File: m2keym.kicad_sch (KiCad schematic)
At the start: 14 parts, among them J7 Bus_M.2_1-2199230-6

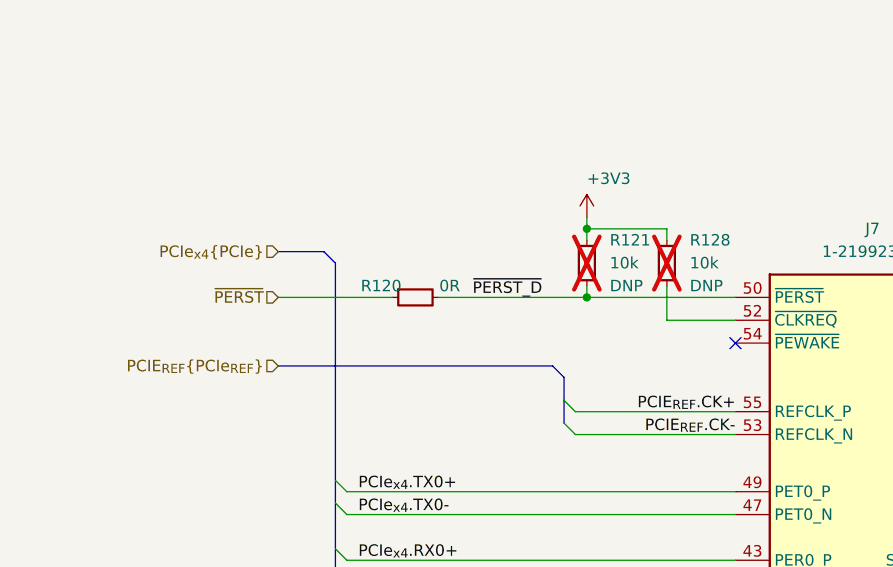
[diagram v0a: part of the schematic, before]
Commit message: [#58904] Change pinout of backplane connector. Connect CLKREQ from PCIe devices
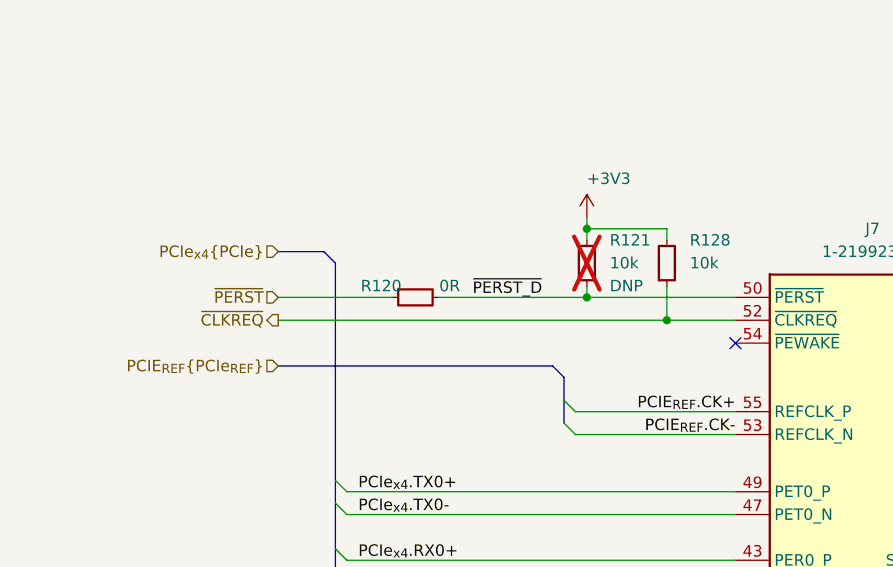
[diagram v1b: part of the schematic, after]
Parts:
- R128: DNP DNP -> (none); now fitted
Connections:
- net ~{CLKREQ}: now reaches J7.52 (~{CLKREQ}), R128.1
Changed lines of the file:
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@@
     (company "Antmicro Ltd.")
+  )
+  (junction (at 193.04 91.44) (diameter 0) (color 0 0 0 0)
   )
   (junction (at 184.15 81.28) (diameter 0) (color 0 0 0 0)
@@
     (stroke (width 0) (type default))
   )
+  (wire (pts (xy 149.86 91.44) (xy 193.04 91.44))
+    (stroke (width 0) (type default))
+  )
   (bus (pts (xy 156.21 134.62) (xy 156.21 139.7))
     (stroke (width 0) (type default))
@@
   )
   (hierarchical_label "PCIe_{x4}{PCIe}" (shape input) (at 149.86 83.82 180) (fields_autoplaced)
+    (effects (font (size 1.27 1.27)) (justify right))
+  )
+  (hierarchical_label "~{CLKREQ}" (shape output) (at 149.86 91.44 180) (fields_autoplaced)
     (effects (font (size 1.27 1.27)) (justify right))
   )
@@
   )
   (symbol (lib_id "antmicroResistors0402:R_10k_0402") (at 193.04 87.63 90) (unit 1)
-    (in_bom yes) (on_board yes) (dnp yes) (fields_autoplaced)
+    (in_bom yes) (on_board yes) (dnp no) (fields_autoplaced)
     (property "Reference" "R128" (at 195.58 82.55 90)
       (effects (font (size 1.27 1.27) (thickness 0.15)) (justify right))
@@
       (effects (font (size 1.27 1.27)) (justify left bottom) hide)
     )
-    (property "DNP" "DNP" (at 195.58 87.63 90)
-      (effects (font (size 1.27 1.27)) (justify right))
-    )
     (pin "2")

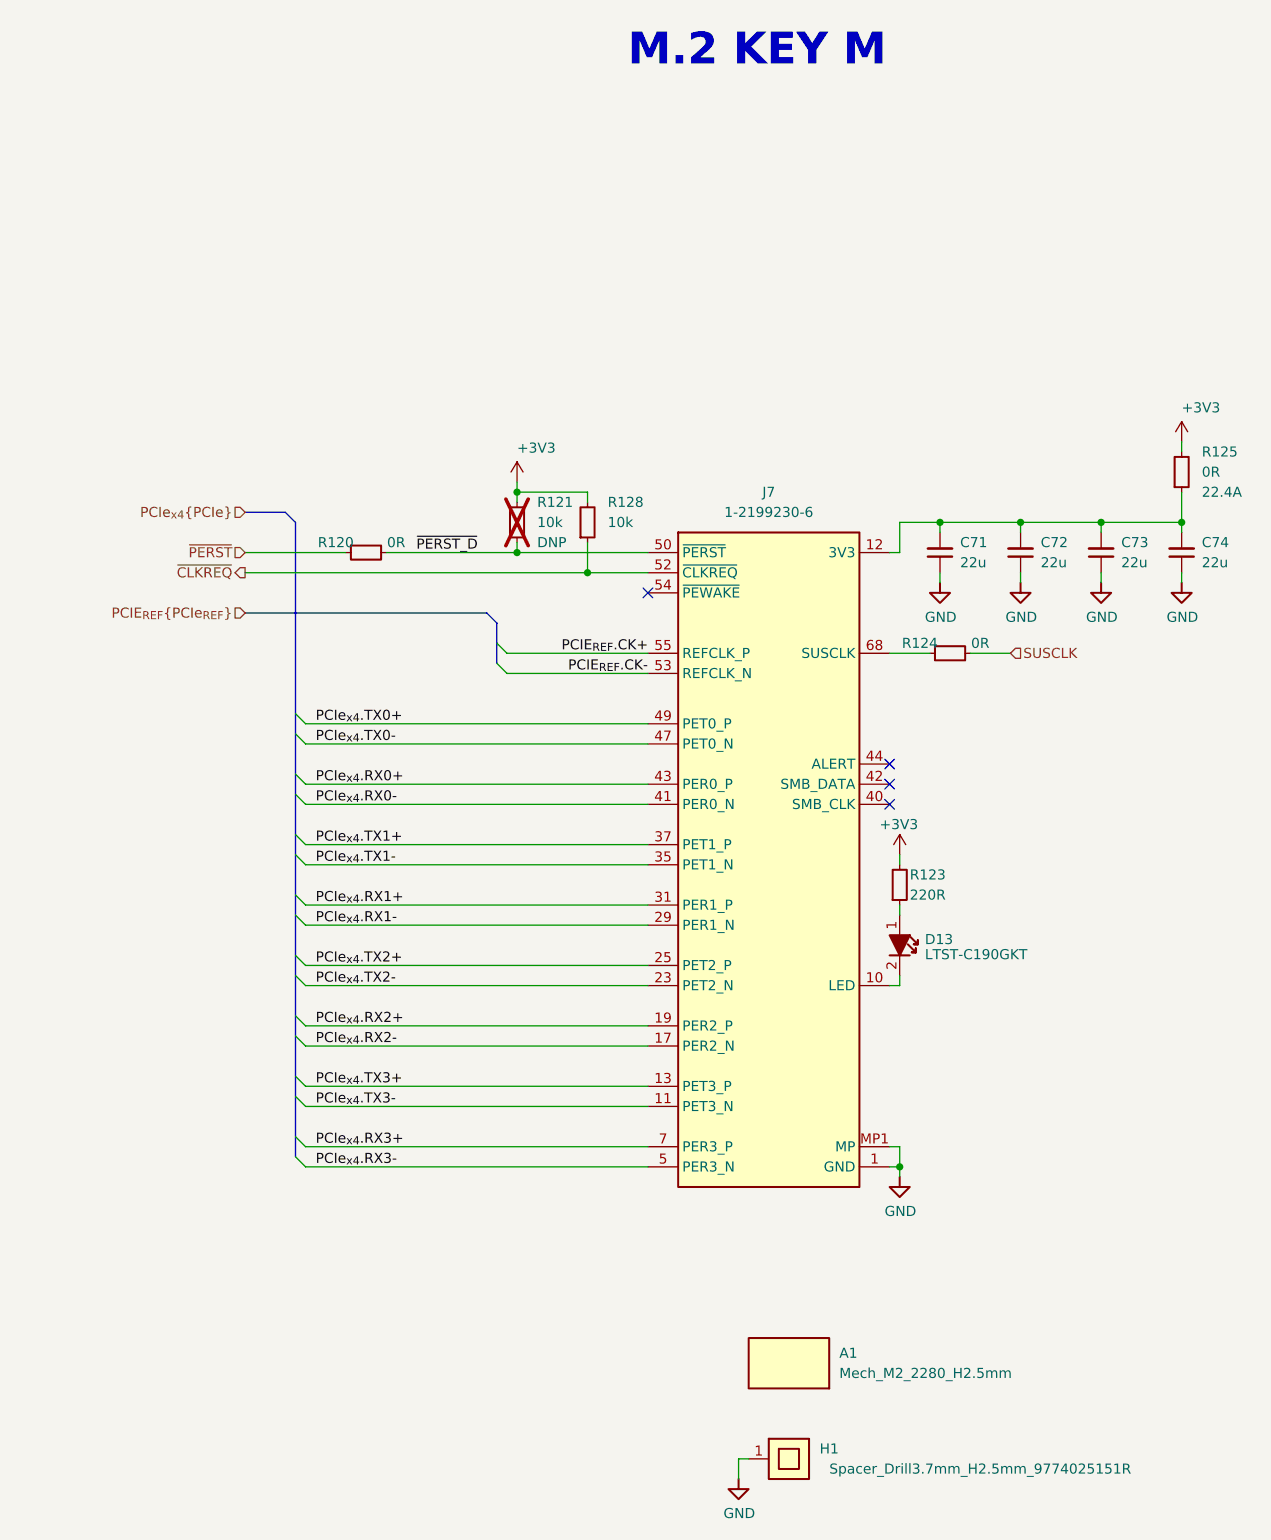
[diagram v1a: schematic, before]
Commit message: Update components from the library
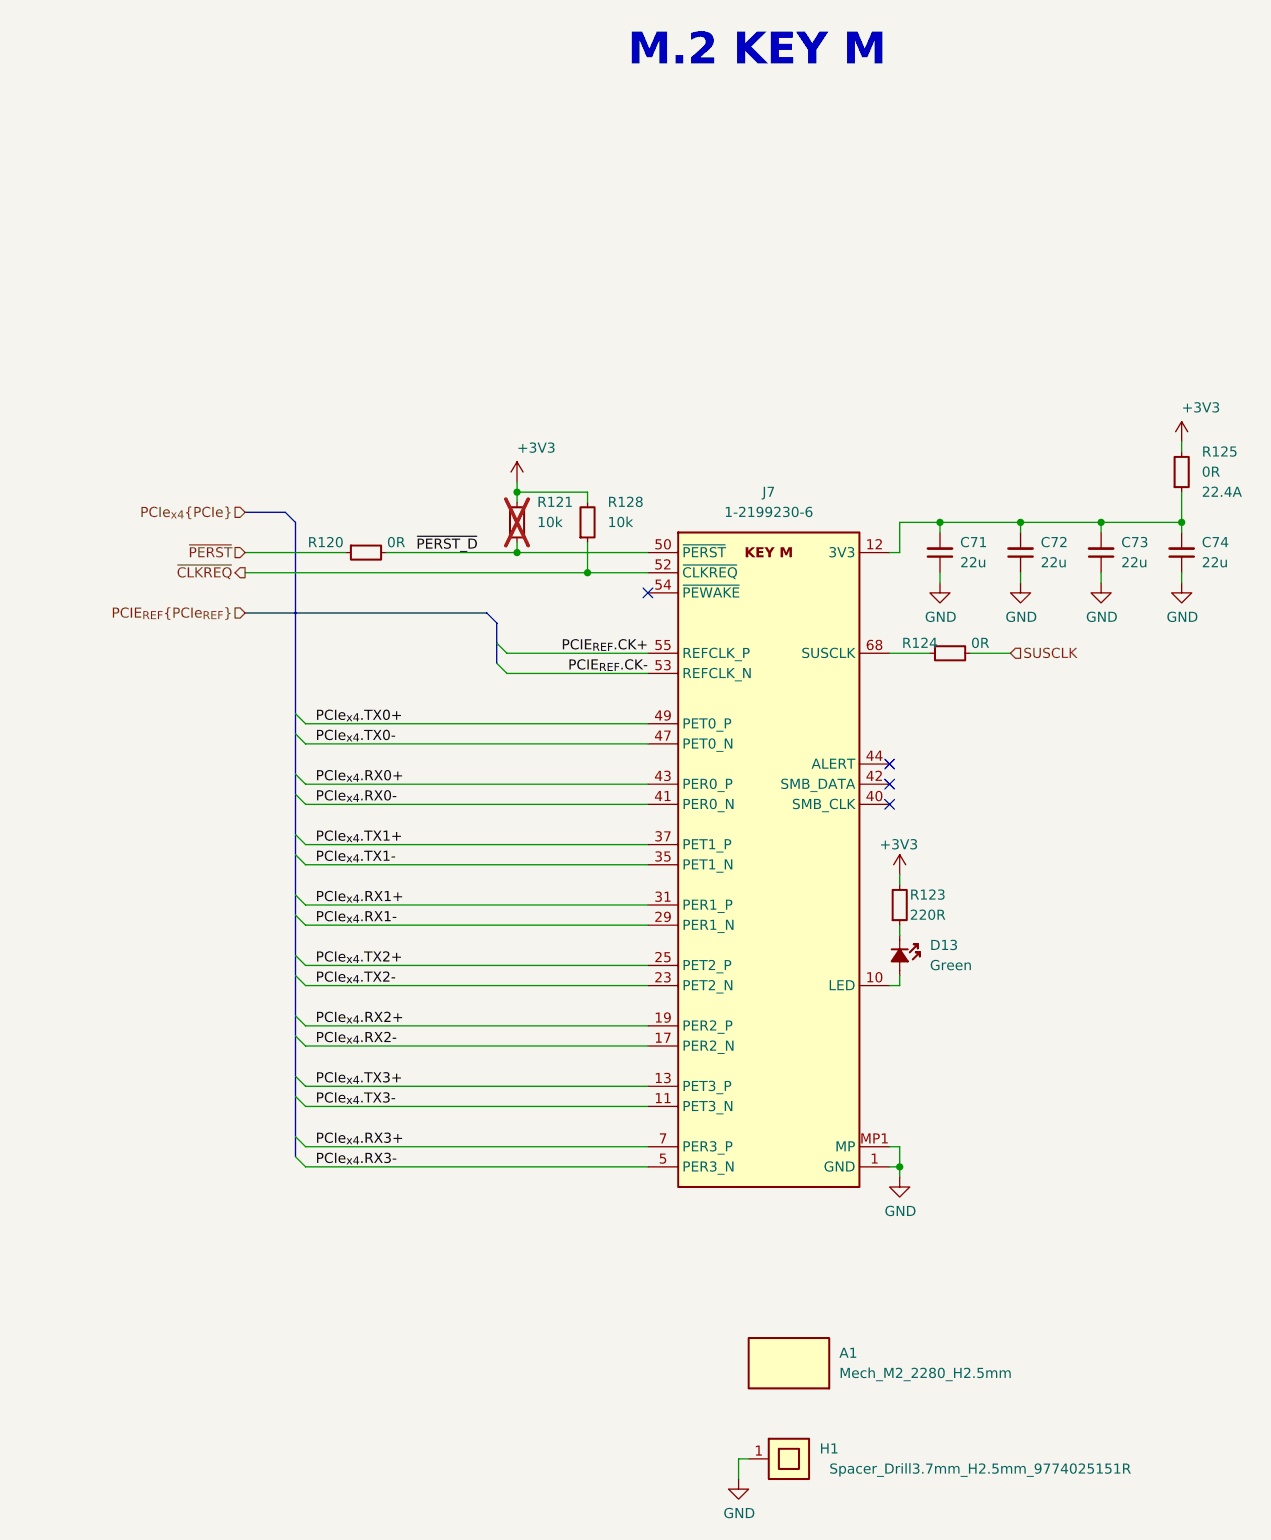
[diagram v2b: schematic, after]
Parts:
- A1, C71, C72, C73, C74, H1, R120, R123, R124, R125, R128: Public (none) -> False
- D13: Color (none) -> Green; Manufacturer Lite-On Inc. -> Lite-On; Public (none) -> False
- R121: DNP DNP -> (none); Public (none) -> False
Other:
- moved on the sheet: D13, R123

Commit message: [#65446] Add low profile M.2 key M connector, move M.2 drives
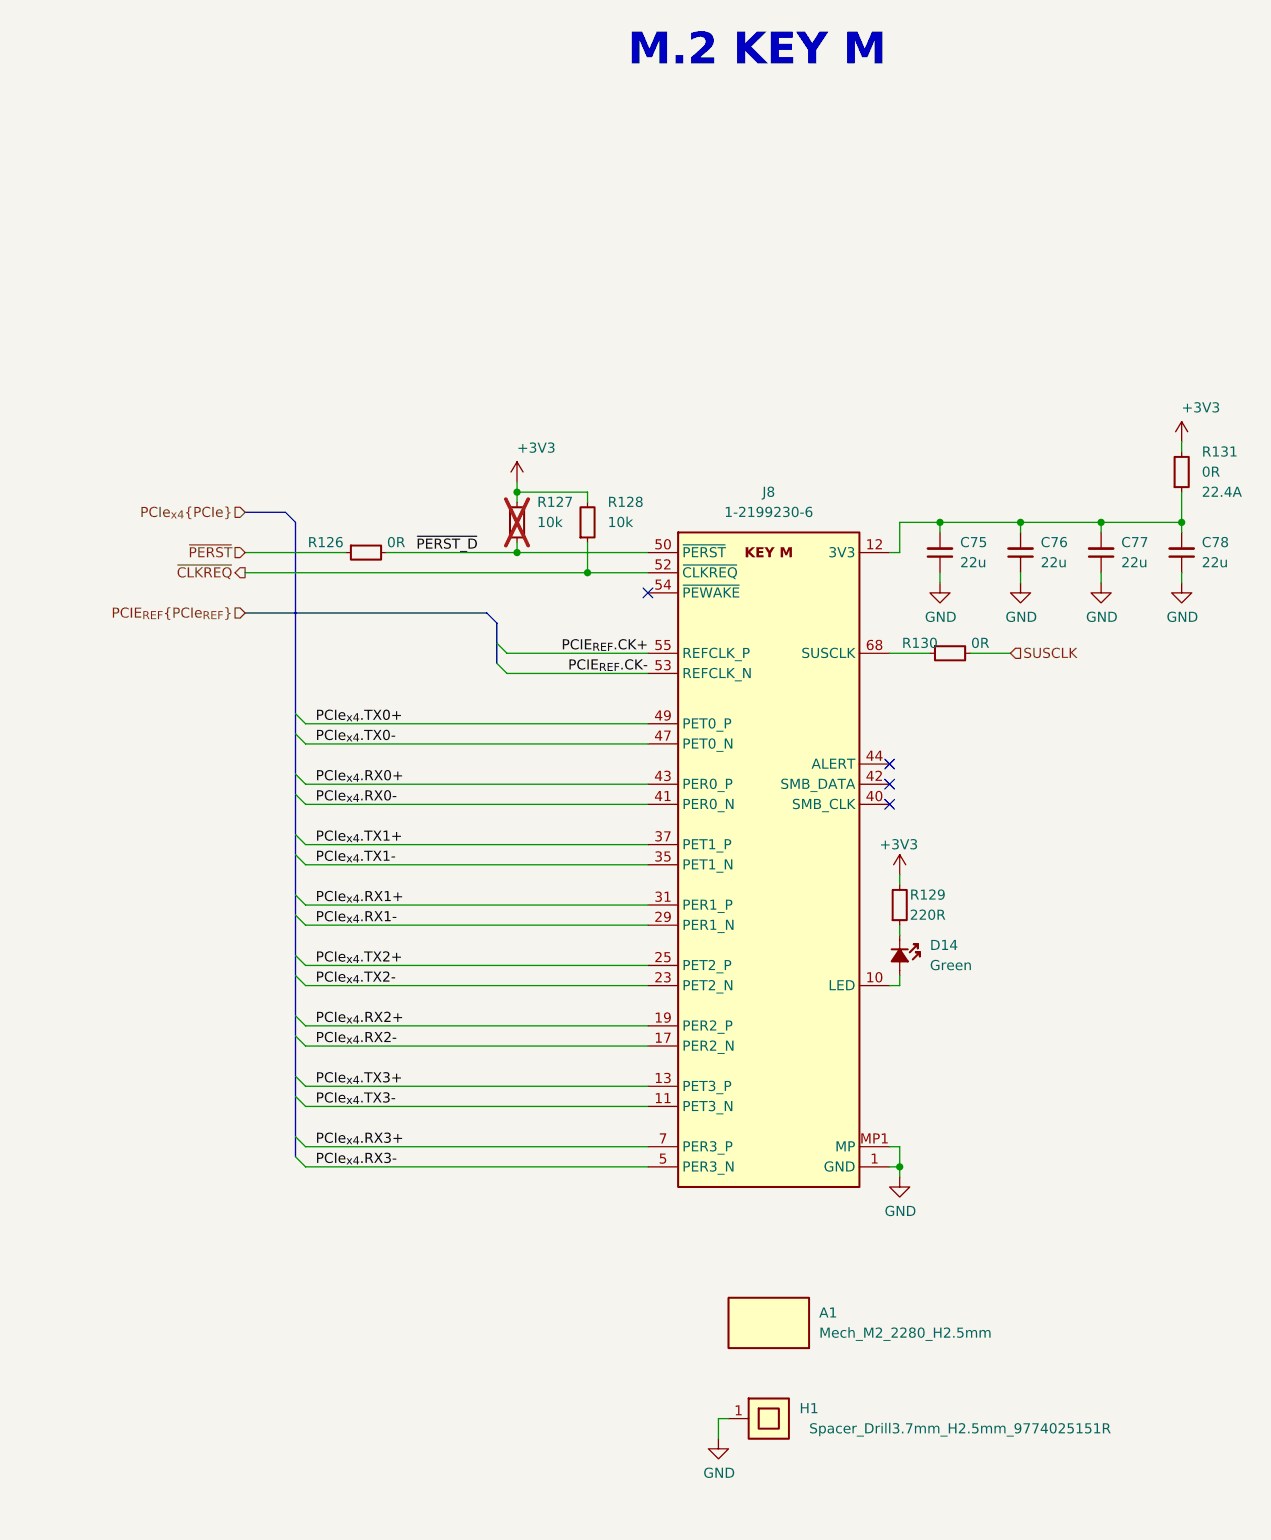
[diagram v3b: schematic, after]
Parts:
- renumbered C71 to C75, C72 to C76, C73 to C77, C74 to C78, D13 to D14, J7 to J8, R120 to R126, R121 to R127, R123 to R129, R124 to R130, R125 to R131
